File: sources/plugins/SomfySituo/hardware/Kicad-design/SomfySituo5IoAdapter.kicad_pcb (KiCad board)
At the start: 2 copper layers, 25.4 x 21.8 mm, 30 parts, among them J1 USB_OTG, J10 Conn_01x01, J11 Conn_01x01, J12 Conn_01x01, J13 Conn_01x01, J15 ICSP, J2 Conn_01x01, J3 Conn_01x01, J4 Conn_01x01, J5 Conn_01x01, J6 Conn_01x01, J7 Conn_01x01, J8 Conn_01x01, J9 Conn_01x01, U1 FT230X, U2 PIC16F688

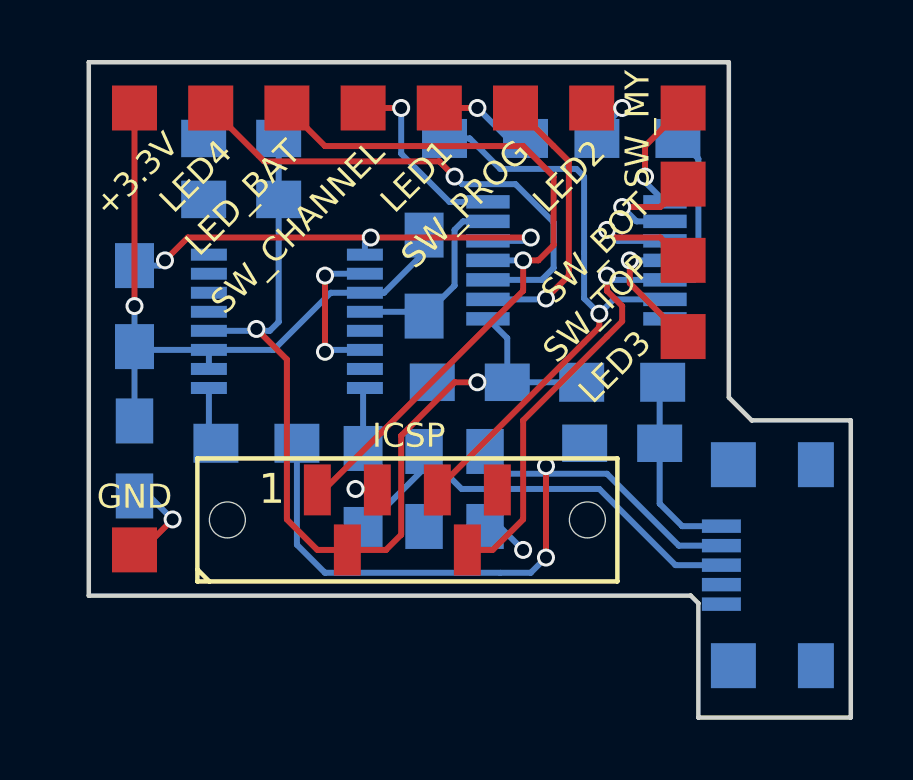
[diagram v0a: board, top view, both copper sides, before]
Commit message: Fix output leds and serigraphy
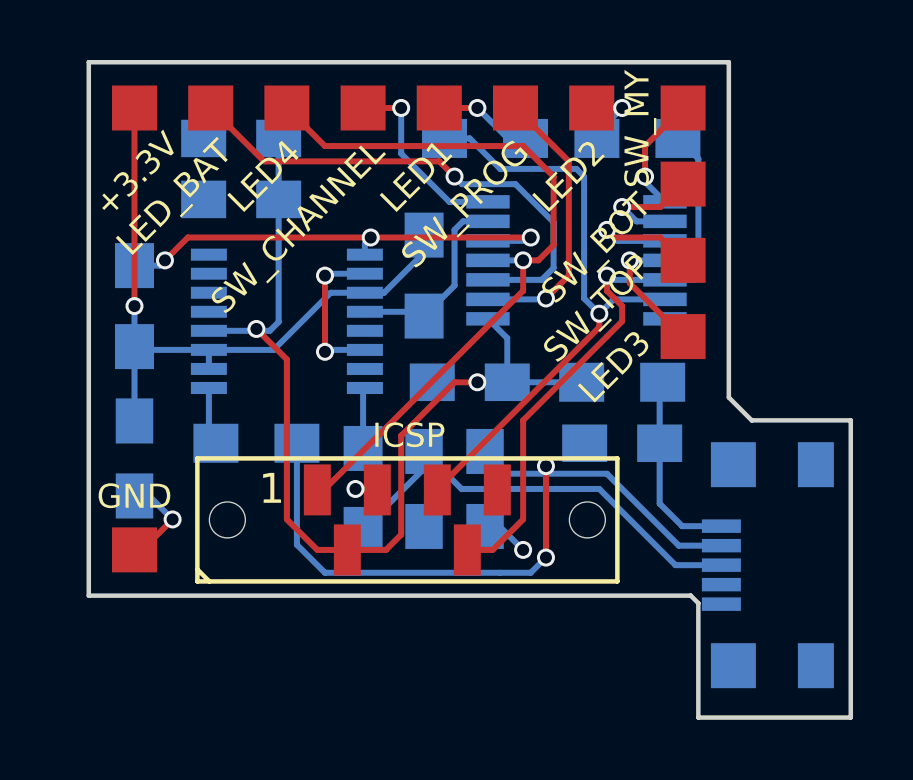
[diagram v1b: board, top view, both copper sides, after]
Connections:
- net Somfy_led4 renamed Somfy_led_battery
